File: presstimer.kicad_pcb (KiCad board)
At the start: 2 copper layers, 63 parts, among them J1 Screw_Terminal_01x02, J10 Conn_01x06_Pin, J2 Conn_ARM_SWD_TagConnect_TC2030, J3 Connector, USB-TYPE-C-16P, J4 Screw_Terminal_01x02, J5 Screw_Terminal_01x02, J6 Screw_Terminal_01x03, J7 Screw_Terminal_01x02, J8 Conn_01x06_Pin, J9 Conn_01x06_Pin, Q5 Display 2.8" TFT LCD Touch IL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, Q6 AO3401A, Q7 2SC1623, SW1 SW_Push, SW2 SW_Push, U1 AP7361C-33ER, U2 ESP32-S3-WROOM-1, U3 SFH620A-3X001, U4 SFH620A-3X001, U5 SSR-41FDD

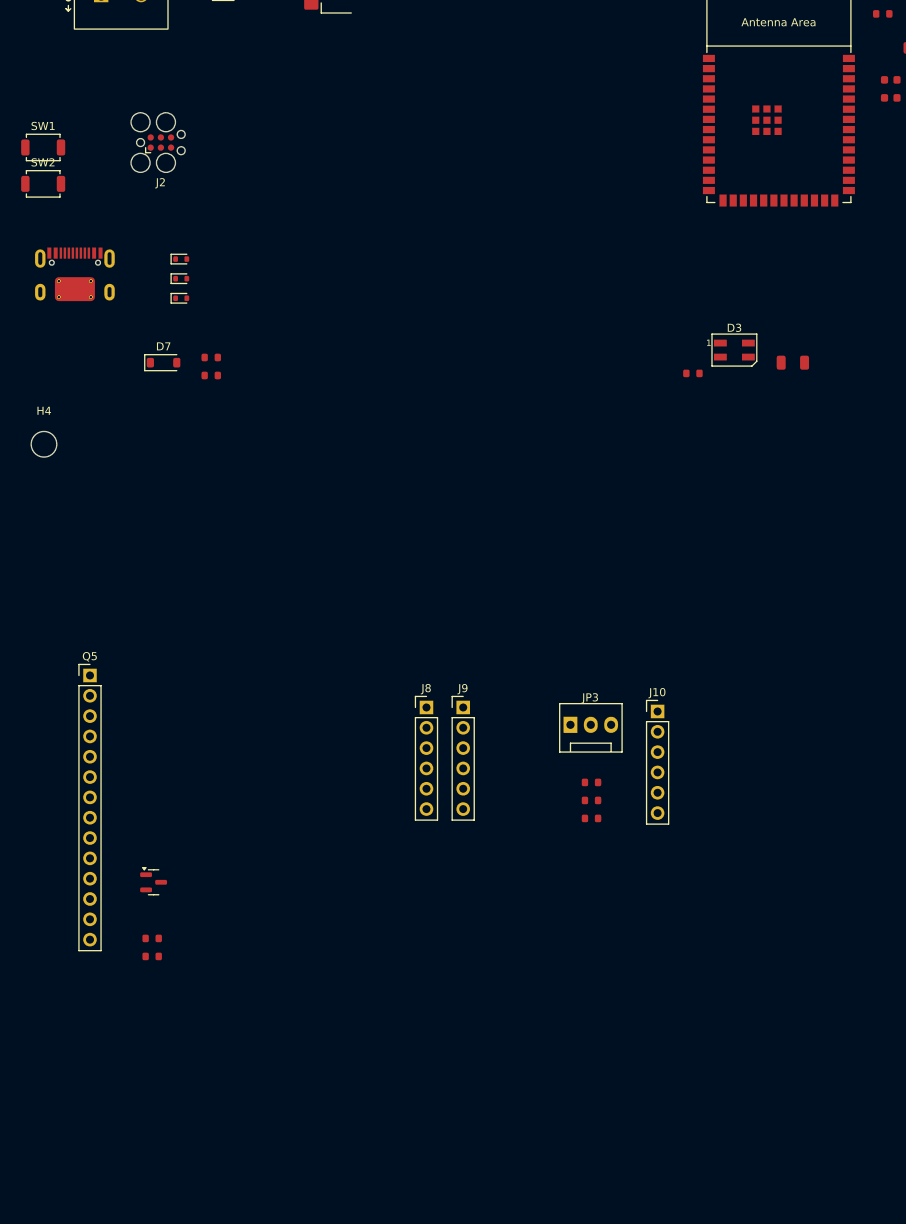
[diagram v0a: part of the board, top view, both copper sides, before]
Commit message: added usb-serial programmer and footprints
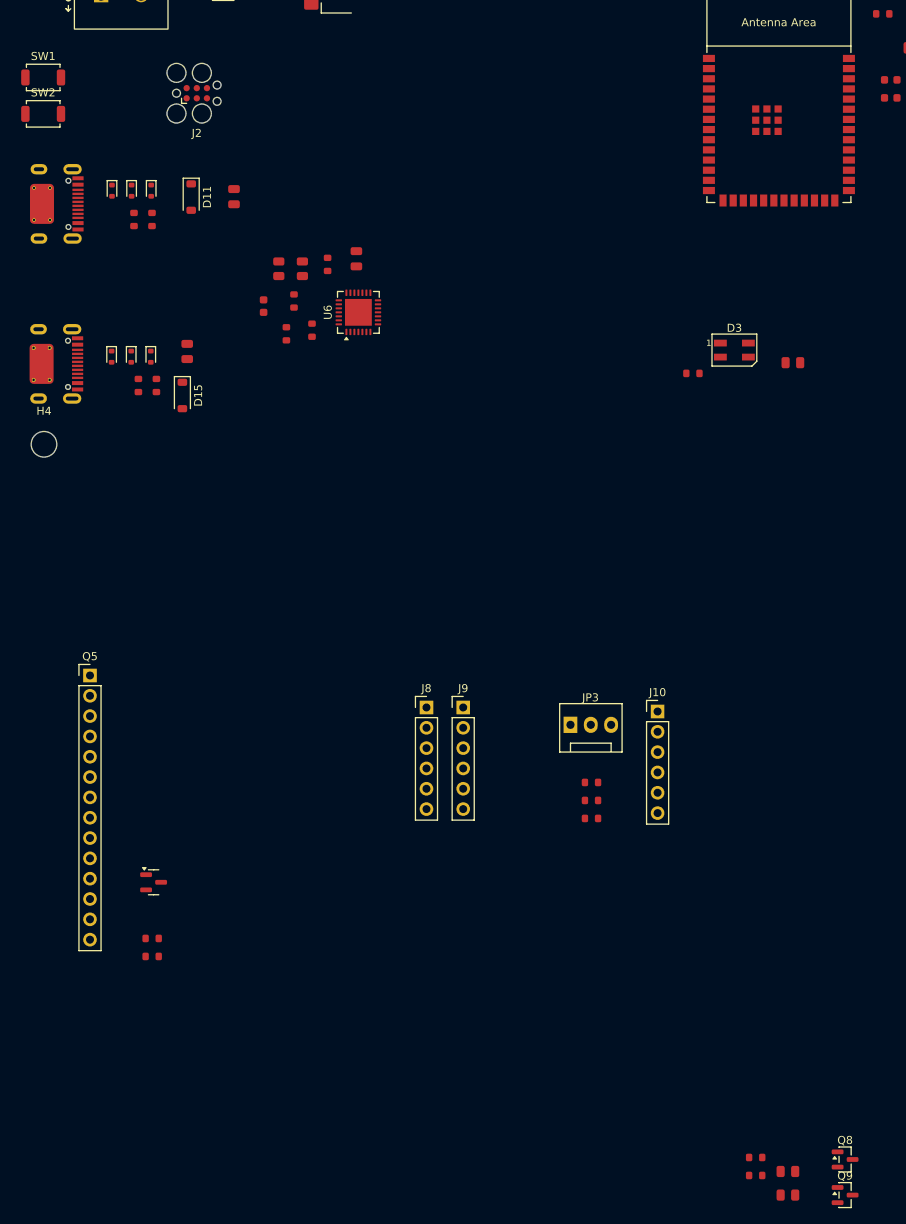
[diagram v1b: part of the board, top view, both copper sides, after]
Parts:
- removed D6, D8, D9: LESD5D5.0CT1G, PCM_JLCPCB:D_SOD-523
- removed D7: 1N5819HW-7-F, Diode_SMD:D_SOD-123
- removed J3: Connector, USB-TYPE-C-16P, PCM_JLCPCB:TYPE-C-SMD_HX-TYPE-C-16PIN
- removed R13, R14: 5k1, PCM_JLCPCB:R_0603
- added C11: 22uF, PCM_JLCPCB:C_0805, F.Cu at (44.1, 52.4)
- added C12: 22uF, PCM_JLCPCB:C_0805, F.Cu at (38.3, 71.8)
- added C13: 1uF, PCM_JLCPCB:C_0603, F.Cu at (47.9, 66.1)
- added C14: 10uF, PCM_JLCPCB:C_0805, F.Cu at (59.5, 60.2)
- added D10: LESD5D5.0CT1G, PCM_JLCPCB:D_SOD-523, F.Cu at (33.8, 51.6)
- added D11: 1N5819HW-7-F, Diode_SMD:D_SOD-123, F.Cu at (38.8, 52.5)
- added D12: LESD5D5.0CT1G, PCM_JLCPCB:D_SOD-523, F.Cu at (31.4, 51.6)
- added D13: LESD5D5.0CT1G, PCM_JLCPCB:D_SOD-523, F.Cu at (28.9, 51.6)
- added D14: LESD5D5.0CT1G, PCM_JLCPCB:D_SOD-523, F.Cu at (33.8, 72.4)
- added D15: 1N5819HW-7-F, Diode_SMD:D_SOD-123, F.Cu at (37.7, 77.2)
- added D16: LESD5D5.0CT1G, PCM_JLCPCB:D_SOD-523, F.Cu at (31.3, 72.4)
- added D17: LESD5D5.0CT1G, PCM_JLCPCB:D_SOD-523, F.Cu at (28.9, 72.4)
- added J11: Connector, USB-TYPE-C-16P, PCM_JLCPCB:TYPE-C-SMD_HX-TYPE-C-16PIN, F.Cu at (22.1, 53.3)
- added J12: Connector, USB-TYPE-C-16P, PCM_JLCPCB:TYPE-C-SMD_HX-TYPE-C-16PIN, F.Cu at (22.1, 73.3)
- added Q8: L8050QLT1G, Package_TO_SOT_SMD:SOT-23, F.Cu at (120.5, 172.8)
- added Q9: L8050QLT1G, Package_TO_SOT_SMD:SOT-23, F.Cu at (120.5, 177.2)
- added R23: 5k1, PCM_JLCPCB:R_0603, F.Cu at (33.9, 55.2)
- added R24: 5k1, PCM_JLCPCB:R_0603, F.Cu at (31.6, 55.2)
- added R32: 10k, PCM_JLCPCB:R_0603, F.Cu at (53.9, 69.1)
- added R33: 5k1, PCM_JLCPCB:R_0603, F.Cu at (34.5, 76.0)
- added R34: 5k1, PCM_JLCPCB:R_0603, F.Cu at (32.2, 76.0)
- added R35: 22k1, PCM_JLCPCB:R_0603, F.Cu at (55.9, 60.9)
- added R36: 47k5, PCM_JLCPCB:R_0603, F.Cu at (50.7, 69.5)
- added R37: 1k, PCM_JLCPCB:R_0603, F.Cu at (51.6, 65.4)
- added R38: 0, PCM_JLCPCB:R_0805, F.Cu at (49.8, 61.4)
- added R39: 0, PCM_JLCPCB:R_0805, F.Cu at (52.7, 61.4)
- added R40: 10k, PCM_JLCPCB:R_0603, F.Cu at (109.4, 172.5)
- added R41: 10k, PCM_JLCPCB:R_0603, F.Cu at (109.4, 174.8)
- added R42: 0, PCM_JLCPCB:R_0805, F.Cu at (113.4, 174.2)
- added R43: 0, PCM_JLCPCB:R_0805, F.Cu at (113.4, 177.2)
- added U6: CP2102N-Axx-xQFN28, Package_DFN_QFN:QFN-28-1EP_5x5mm_P0.5mm_EP3.35x3.35mm, F.Cu at (59.7, 66.9)
- R25: footprint PCM_JLCPCB:R_1206 -> PCM_JLCPCB:R_0805
- moved SW1 8.75 mm to (20.3, 37.5)
- moved SW2 8.75 mm to (20.3, 42.0)
- moved J2 7.63 mm to (39.5, 39.5)

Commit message: before restore, crashed session
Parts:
- removed Q7: 2SC1623, PCM_JLCPCB:Q_SOT-23
- added Q10: L8050QLT1G, Package_TO_SOT_SMD:SOT-23, F.Cu at (201.1, 35.4)
- renumbered C12 to C10, C13 to C12, C14 to C13, C5 to C3, C3 to C4, C4 to C5, C9 to C7, C7 to C8, C8 to C9, D17 to D10, D3 to D2, D10 to D3, D14 to D4, D11 to D5, D15 to D6, D12 to D7, D16 to D8, D13 to D9, J7 to J10, J12 to J11, J6 to J2, J11 to J3, J2 to J4, J8 to J5, J9 to J6, J10 to J7, J4 to J8, J5 to J9, R3 to R1, R19 to R10, R26 to R13, R2 to R14, R17 to R15, R20 to R16, R21 to R17, R27 to R18, R28 to R19, R4 to R2, R29 to R20, R22 to R21, R9 to R22, R33 to R24, R24 to R25, R34 to R26, R15 to R27, R10 to R28, R16 to R29, R1 to R3, R40 to R30, R41 to R31, R35 to R32, R42 to R33, R36 to R34, R43 to R35, R37 to R36, R32 to R37, R25 to R4, R18 to R9

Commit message: parts assigned, footprints checked
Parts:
- Q6: footprint PCM_JLCPCB:Q_SOT-23 -> Package_TO_SOT_SMD:SOT-23
- moved Q8 38.9 mm to (149.6, 146.8)
- moved R30 38.9 mm to (138.4, 146.6)
- moved R31 38.9 mm to (138.4, 148.8)
- moved R33 38.9 mm to (142.4, 148.3)
- moved Q9 38.9 mm to (149.6, 151.3)
- moved R35 38.9 mm to (142.4, 151.3)
- moved J1 25.5 mm to (49.2, 28.6), turned to 180 degrees
- moved F1 23.7 mm to (54.1, 27.5), turned to 90 degrees
- moved J9 22.1 mm to (248.1, 87.0), turned to 90 degrees
- moved J10 19.5 mm to (252.2, 44.7), turned to 90 degrees
- moved J8 19.0 mm to (253.7, 67.1), turned to 90 degrees
- moved C13 13.4 mm to (71.0, 67.0)
- moved R13 13.4 mm to (113.1, 81.3)
- moved R36 13.4 mm to (63.2, 72.3)
- moved R38 13.4 mm to (61.3, 68.2)
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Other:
- board outline added: 251.6 x 144.2 mm

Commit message: started pcb layout
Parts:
- removed J7: Conn_01x06_Pin, Connector_PinHeader_2.54mm:PinHeader_1x06_P2.54mm_Vertical
- removed JP3: Jumper_3_Open, Connector:FanPinHeader_1x03_P2.54mm_Vertical
- removed R18, R19, R20: 10k, PCM_JLCPCB:R_0603
- removed R33, R35: 0, PCM_JLCPCB:R_0805
- moved J10 164.9 mm to (122.4, 146.5), turned to 0 degrees
- moved J4 164.5 mm to (186.8, 139.3), turned to -90 degrees
- moved U5 152.2 mm to (105.3, 138.4)
- moved J11 151.0 mm to (184.6, 85.0), turned to 180 degrees
- moved D8 143.1 mm to (185.1, 95.2), turned to 180 degrees
- moved D10 143.0 mm to (182.8, 93.7), turned to 0 degrees
- moved R24 142.9 mm to (188.4, 94.2)
- moved D4 142.8 mm to (187.7, 89.8), turned to 180 degrees
- moved C10 140.0 mm to (187.8, 102.3), turned to 0 degrees
- moved R21 139.9 mm to (116.8, 130.3), turned to -90 degrees
- moved D6 138.5 mm to (187.1, 98.5), turned to 90 degrees
- moved R26 138.1 mm to (181.7, 90.9), turned to 180 degrees
- moved SW1 137.8 mm to (149.2, 116.6), turned to -90 degrees
- moved Q10 134.4 mm to (114.2, 133.7), turned to -90 degrees
- moved SW2 130.8 mm to (143.7, 116.6), turned to -90 degrees
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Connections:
- C1 pad 2: +3V3 -> GND
- C10 pad 2: +3V3 -> GND
- C11 pad 2: +3V3 -> GND
- C12 pad 2: +3V3 -> GND
- C13 pad 2: +3V3 -> GND
- C2 pad 2: +3V3 -> GND
- C3 pad 2: +3V3 -> GND
- C4 pad 2: +3V3 -> GND
- C5 pad 2: +3V3 -> GND
- C7 pad 2: +3V3 -> GND
- C8 pad 2: +3V3 -> GND
- C9 pad 2: +3V3 -> GND
- D10 pad 1: +3V3 -> GND
- D2 pad 2: +3V3 -> GND
- D3 pad 1: +3V3 -> GND
- D4 pad 1: +3V3 -> GND
- D7 pad 1: +3V3 -> GND
- D8 pad 1: +3V3 -> GND
- D9 pad 1: +3V3 -> GND
- J1 pad 2: +3V3 -> GND
- J11 pad A12B1: +3V3 -> GND
- J11 pad B12A1: +3V3 -> GND
- J11 pad S1: +3V3 -> GND
- J2 pad 3: +3V3 -> GND
- J3 pad A12B1: +3V3 -> GND
- J3 pad B12A1: +3V3 -> GND
- J3 pad S1: +3V3 -> GND
- J4 pad 5: +3V3 -> GND
- J5 pad 2: +3V3 -> GND
- J6 pad 6: +3V3 -> GND
- Q10 pad 2: +3V3 -> GND
- Q5 pad 13: +3V3 -> GND
- Q8 pad 3: Net-(Q8-C) -> CHIP_PU
- Q9 pad 2: Net-(Q9-E) -> BOOT
- R10 pad 2: +3V3 -> GND
- R23 pad 2: +3V3 -> GND
- R24 pad 2: +3V3 -> GND
- R25 pad 2: +3V3 -> GND
- R26 pad 2: +3V3 -> GND
- R3 pad 2: +3V3 -> GND
- R34 pad 2: +3V3 -> GND
- R37 pad 1: +3V3 -> GND
- SW1 pad 2: +3V3 -> GND
- SW2 pad 2: +3V3 -> GND
- U1 pad 1: +3V3 -> GND
- U1 pad 4: OUT -> Net-(D1-A)
- U2 pad 1: +3V3 -> GND
- U3 pad 3: +3V3 -> GND
- U4 pad 3: +3V3 -> GND
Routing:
- net GND: track 0.00 -> 22.4 mm
- net Net-(J9-Pin_2): track 0.00 -> 20.8 mm
- net Net-(J8-Pin_2): track 0.00 -> 20.8 mm
- net Net-(D1-A): track 0.00 -> 17.8 mm
- net Net-(U6-VBUS): track 0.00 -> 17.2 mm
- net VBUSB2: track 0.00 -> 13.7 mm
- net Net-(J10-Pin_1): track 0.00 -> 13.1 mm
- net Net-(J10-Pin_2): track 0.00 -> 13.1 mm
- net +3V3: track 0.00 -> 12.2 mm
- net VBUSB: track 0.00 -> 11.2 mm
- net Net-(J1-Pin_1): track 0.00 -> 9.86 mm
- net Net-(J8-Pin_1): track 0.00 -> 7.77 mm
- net Net-(J9-Pin_1): track 0.00 -> 7.52 mm
- net CHIP_PU: track 0.00 -> 6.99 mm
- net Net-(R27-Pad2): track 0.00 -> 5.90 mm
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- added copper zone on B.Cu, net GND
- added copper zone on F.Cu, net GND
- added copper zone on In1.Cu, net GND
- added copper zone on In2.Cu, net GND
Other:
- board size 251.6 x 144.2 mm -> 93 x 76 mm
- copper layers 2 -> 4

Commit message: pcb layout v0.0.2
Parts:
- removed JP1, JP2: Jumper_2_Open, Connector_PinHeader_2.54mm:PinHeader_1x02_P2.54mm_Vertical
- added R5: 0, PCM_JLCPCB:R_0603, F.Cu at (164.0, 88.1)
- added R6: 0, PCM_JLCPCB:R_0603, F.Cu at (164.0, 85.8)
- moved J5 82.5 mm to (174.9, 83.0), turned to -90 degrees
- moved R1 76.9 mm to (166.7, 86.9), turned to -90 degrees
- moved J2 73.1 mm to (107.5, 114.3), turned to -90 degrees
- moved C7 67.5 mm to (109.3, 129.9), turned to 90 degrees
- moved R9 66.4 mm to (109.5, 122.6), turned to 90 degrees
- moved R2 64.9 mm to (161.1, 86.8), turned to 90 degrees
- moved R10 64.6 mm to (111.3, 120.9), turned to 90 degrees
- moved R15 63.2 mm to (111.3, 124.2), turned to 90 degrees
- moved SW1 33.5 mm to (173.2, 93.3), turned to 90 degrees
- moved SW2 30.1 mm to (162.8, 93.3), turned to 90 degrees
- moved H2 29.0 mm to (157.9, 147.2)
- moved R28 24.1 mm to (162.9, 130.2), turned to 0 degrees
- moved C8 20.6 mm to (166.1, 130.2), turned to 0 degrees
- moved U3 16.6 mm to (165.0, 140.9), turned to 90 degrees
- moved J8 16.1 mm to (183.0, 149.8), turned to 90 degrees
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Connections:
- U1 pad 4: Net-(D1-A) -> OUT
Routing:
- net USB_ESP_DP: track 1.70 -> 36.4 mm
- net USB2_DP: track 0.00 -> 34.2 mm, vias 0 -> 2
- net USB_ESP_DN: track 1.70 -> 35.2 mm
- net USB2_DN: track 0.00 -> 32.7 mm, vias 0 -> 2
- net DTR: track 0.00 -> 15.1 mm, vias 0 -> 2
- net RTS: track 0.00 -> 11.0 mm, vias 0 -> 2
- net Net-(J11-CC1): track 0.00 -> 6.91 mm, vias 0 -> 2
- net Net-(J11-CC2): track 0.00 -> 6.27 mm
- net Net-(Q9-B): track 0.00 -> 5.27 mm
- net Net-(U6-RXD): track 0.00 -> 3.64 mm
- net Net-(Q8-B): track 0.00 -> 3.35 mm
- net Net-(U6-TXD): track 0.00 -> 3.10 mm
- net Net-(J3-CC1): track 2.02 -> 0.00 mm
- net Net-(J2-Pin_2): track 0.00 -> 0.86 mm
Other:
- board size 93 x 76 mm -> 93 x 72 mm

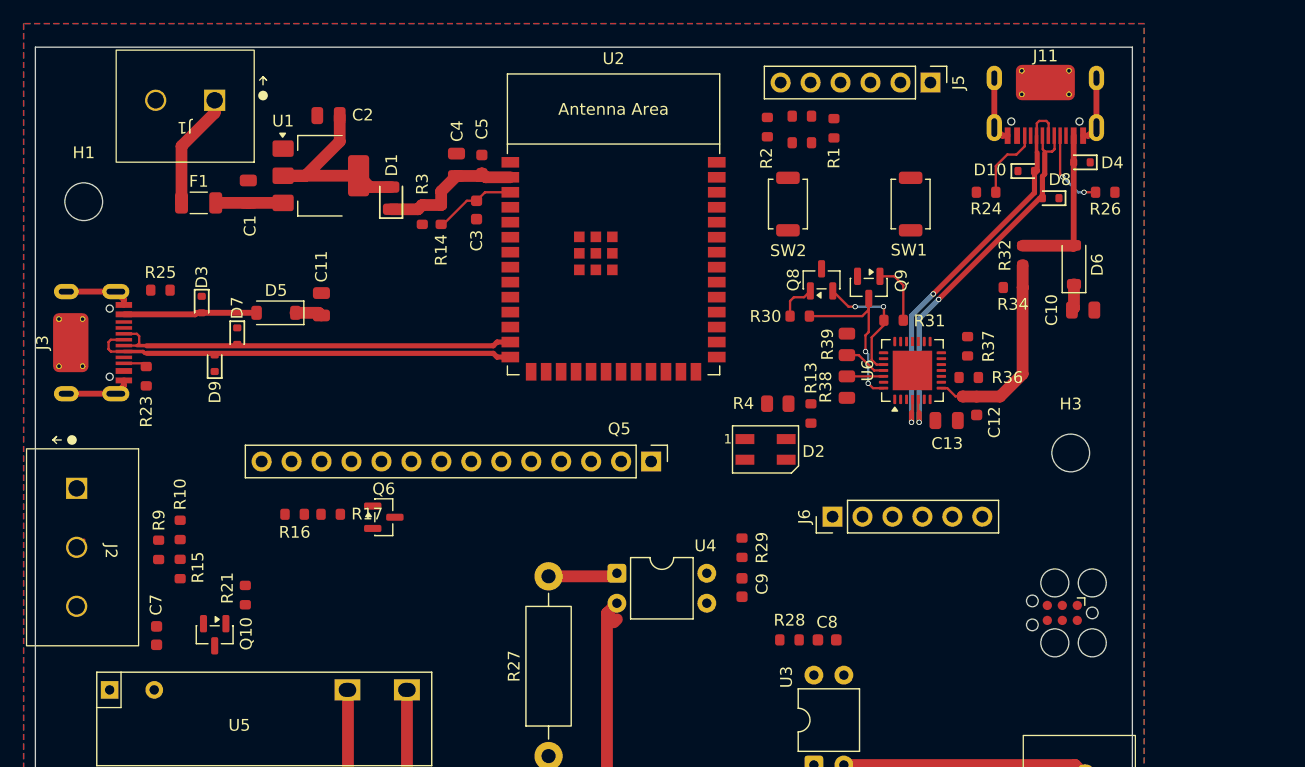
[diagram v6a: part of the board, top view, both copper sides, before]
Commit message: pcb layout v0.0.3 (i forgot the second signal layer ;(.
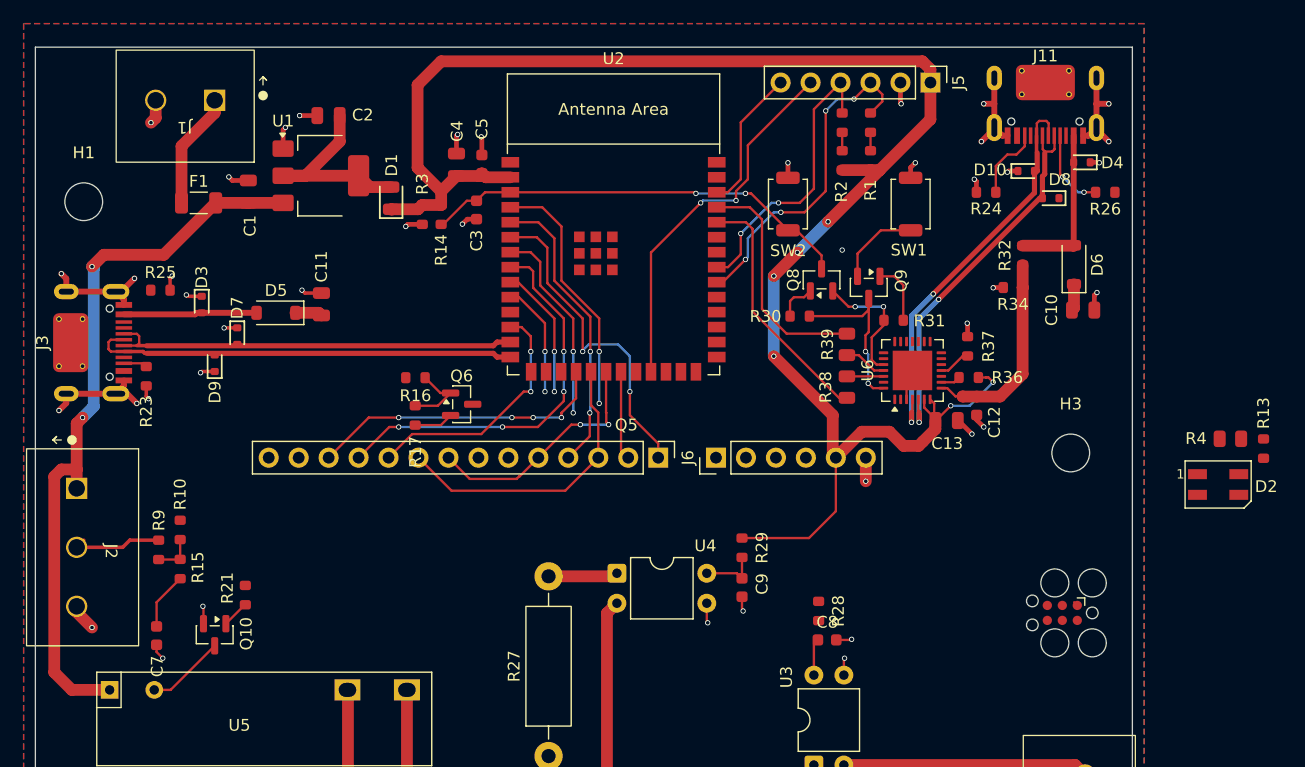
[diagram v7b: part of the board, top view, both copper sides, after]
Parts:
- moved D2 38.5 mm to (199.3, 117.1)
- moved R13 38.5 mm to (203.1, 114.0)
- moved R4 38.5 mm to (200.3, 113.2)
- moved R16 15.5 mm to (131.2, 108.0)
- moved Q6 11.6 mm to (135.1, 110.3)
- moved J6 11.1 mm to (156.7, 114.8)
- moved R17 11.0 mm to (131.2, 111.2), turned to 90 degrees
- moved R2 6.95 mm to (167.4, 89.6)
- moved R5 6.06 mm to (169.8, 86.4), turned to -90 degrees
- moved R1 4.13 mm to (169.8, 89.6)
- moved R28 3.48 mm to (165.4, 127.8), turned to -90 degrees
- moved R6 3.46 mm to (167.4, 86.4), turned to 90 degrees
- moved Q5 0.68 mm to (151.8, 114.8)
- turned C7 to -90 degrees
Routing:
- net +3V3: track 12.2 -> 150.6 mm, vias 0 -> 7
- net GND: track 22.4 -> 83.3 mm, vias 0 -> 41
- net +5V: track 5.71 -> 62.0 mm, vias 0 -> 2
- net D_RST: track 0.00 -> 33.5 mm, vias 0 -> 4
- net I2C_INT: track 0.00 -> 31.8 mm, vias 0 -> 2
- net CHIP_PU: track 6.99 -> 36.7 mm, vias 0 -> 2
- net I2C_SDA: track 0.00 -> 28.4 mm, vias 0 -> 4
- net D_T_IRQ: track 0.00 -> 27.9 mm, vias 0 -> 2
- net D_CS: track 0.00 -> 25.5 mm, vias 0 -> 4
- net D_SDI_T_DIN: track 0.00 -> 25.1 mm
- net D_T_CS: track 0.00 -> 24.9 mm, vias 0 -> 2
- net I2C_SCL: track 0.00 -> 24.8 mm, vias 0 -> 2
- net SENSE_VALVE: track 0.00 -> 21.8 mm, vias 0 -> 2
- net D_BL: track 0.00 -> 21.3 mm, vias 0 -> 2
- net U0RXD: track 0.00 -> 21.3 mm
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
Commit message: start over routing
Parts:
- moved R36 6.40 mm to (178.1, 114.4)
- moved R37 1.14 mm to (178.8, 106.2)
- moved C12 0.80 mm to (178.8, 109.6)
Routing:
- net GND: track 83.3 -> 24.1 mm, vias 41 -> 0
- net +3V3: track 150.6 -> 97.7 mm, vias 7 -> 0
- net D_RST: track 33.5 -> 0.00 mm, vias 4 -> 0
- net I2C_INT: track 31.8 -> 0.00 mm, vias 2 -> 0
- net CHIP_PU: track 36.7 -> 7.72 mm, vias 2 -> 0
- net D_T_IRQ: track 27.9 -> 0.00 mm, vias 2 -> 0
- net I2C_SDA: track 28.4 -> 0.53 mm, vias 4 -> 0
- net D_CS: track 25.5 -> 0.00 mm, vias 4 -> 0
- net D_SDI_T_DIN: track 25.1 -> 0.00 mm
- net D_T_CS: track 24.9 -> 0.00 mm, vias 2 -> 0
- net D_BL: track 21.3 -> 0.00 mm, vias 2 -> 0
- net D_DC: track 21.1 -> 0.00 mm, vias 2 -> 0
- net I2C_SCL: track 24.8 -> 3.79 mm, vias 2 -> 0
- net D_SCK_T_CLK: track 20.8 -> 0.00 mm, vias 2 -> 0
- net U0RXD: track 21.3 -> 0.67 mm
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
